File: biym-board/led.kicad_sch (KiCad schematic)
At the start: 3 parts, among them J3 HEADER_01X04_JST_ZH_SMD_VERTI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

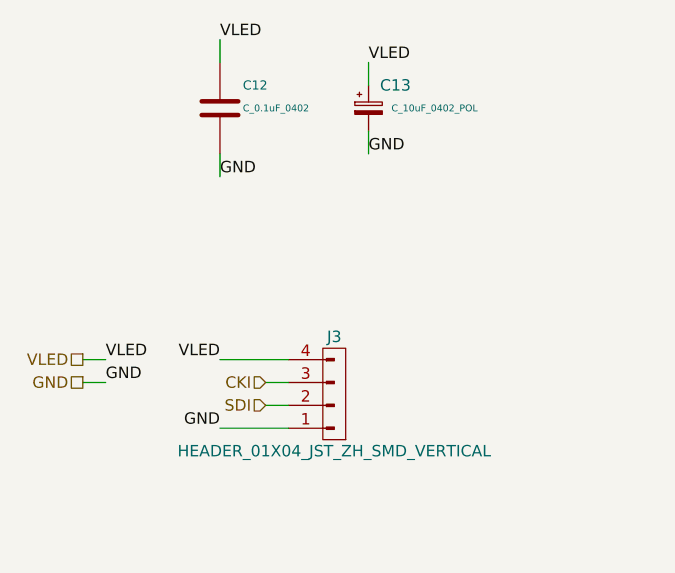
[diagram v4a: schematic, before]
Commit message: Add boost for both led and servo
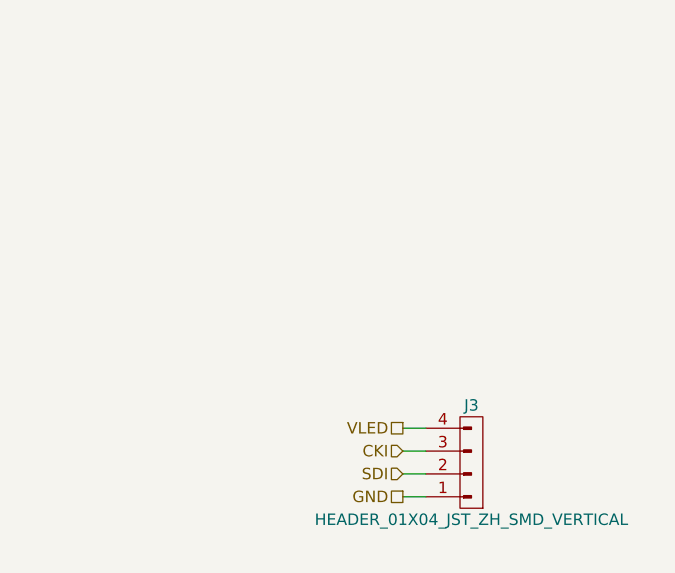
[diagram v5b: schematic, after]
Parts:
- removed C12: C_0.1uF_0402, Janelia:SM0402, symbol Janelia:C_0.1uF_0402
- removed C13: C_10uF_0402_POL, Janelia:SM0402_POL, symbol Janelia:C_10uF_0402_POL
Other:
- moved on the sheet: J3
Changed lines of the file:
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@@
     (company "Peter Polidoro")
   )
-  (wire (pts (xy 119.38 63.5) (xy 119.38 66.04))
+  (wire (pts (xy 139.7 96.52) (xy 142.24 96.52))
     (stroke (width 0) (type default) (color 0 0 0 0))
   )
-  (wire (pts (xy 135.89 60.96) (xy 135.89 63.5))
+  (wire (pts (xy 139.7 93.98) (xy 142.24 93.98))
     (stroke (width 0) (type default) (color 0 0 0 0))
   )
-  (wire (pts (xy 124.46 88.9) (xy 127 88.9))
+  (wire (pts (xy 139.7 99.06) (xy 142.24 99.06))
     (stroke (width 0) (type default) (color 0 0 0 0))
   )
-  (wire (pts (xy 135.89 53.34) (xy 135.89 55.88))
+  (wire (pts (xy 139.7 101.6) (xy 142.24 101.6))
     (stroke (width 0) (type default) (color 0 0 0 0))
   )
-  (wire (pts (xy 104.14 88.9) (xy 106.68 88.9))
-    (stroke (width 0) (type default) (color 0 0 0 0))
-  )
-  (wire (pts (xy 104.14 86.36) (xy 106.68 86.36))
-    (stroke (width 0) (type default) (color 0 0 0 0))
-  )
-  (wire (pts (xy 124.46 91.44) (xy 127 91.44))
-    (stroke (width 0) (type default) (color 0 0 0 0))
-  )
-  (wire (pts (xy 119.38 50.8) (xy 119.38 53.34))
-    (stroke (width 0) (type default) (color 0 0 0 0))
-  )
-  (wire (pts (xy 119.38 86.36) (xy 127 86.36))
-    (stroke (width 0) (type default) (color 0 0 0 0))
-  )
-  (wire (pts (xy 119.38 93.98) (xy 127 93.98))
-    (stroke (width 0) (type default) (color 0 0 0 0))
-  )
-  (label "VLED" (at 135.89 53.34 0)
-    (effects (font (size 1.27 1.27)) (justify left bottom))
-  )
-  (label "VLED" (at 119.38 86.36 180)
-    (effects (font (size 1.27 1.27)) (justify right bottom))
-  )
-  (label "GND" (at 119.38 93.98 180)
-    (effects (font (size 1.27 1.27)) (justify right bottom))
-  )
-  (label "GND" (at 135.89 63.5 0)
-    (effects (font (size 1.27 1.27)) (justify left bottom))
-  )
-  (label "VLED" (at 106.68 86.36 0)
-    (effects (font (size 1.27 1.27)) (justify left bottom))
-  )
-  (label "VLED" (at 119.38 50.8 0)
-    (effects (font (size 1.27 1.27)) (justify left bottom))
-  )
-  (label "GND" (at 119.38 66.04 0)
-    (effects (font (size 1.27 1.27)) (justify left bottom))
-  )
-  (label "GND" (at 106.68 88.9 0)
-    (effects (font (size 1.27 1.27)) (justify left bottom))
-  )
-  (hierarchical_label "VLED" (shape passive) (at 104.14 86.36 180)
+  (hierarchical_label "VLED" (shape passive) (at 139.7 93.98 180)
     (effects (font (size 1.27 1.27)) (justify right))
   )
-  (hierarchical_label "SDI" (shape input) (at 124.46 91.44 180)
+  (hierarchical_label "SDI" (shape input) (at 139.7 99.06 180)
     (effects (font (size 1.27 1.27)) (justify right))
   )
-  (hierarchical_label "GND" (shape passive) (at 104.14 88.9 180)
+  (hierarchical_label "GND" (shape passive) (at 139.7 101.6 180)
     (effects (font (size 1.27 1.27)) (justify right))
   )
-  (hierarchical_label "CKI" (shape input) (at 124.46 88.9 180)
+  (hierarchical_label "CKI" (shape input) (at 139.7 96.52 180)
     (effects (font (size 1.27 1.27)) (justify right))
   )
-  (symbol (lib_id "Janelia:HEADER_01X04_JST_ZH_SMD_VERTICAL") (at 132.08 90.17 180) (unit 1)
+  (symbol (lib_id "Janelia:HEADER_01X04_JST_ZH_SMD_VERTICAL") (at 147.32 97.79 180) (unit 1)
     (in_bom yes) (on_board yes)
-    (property "Reference" "J3" (id 0) (at 132.08 83.82 0))
-    (property "Value" "HEADER_01X04_JST_ZH_SMD_VERTICAL" (id 1) (at 132.08 96.52 0))
-    (property "Footprint" "Janelia:JST_ZH_B4B_ZR_SM4_TF_1x04-1MP_P1.50mm_Vertical" (id 2) (at 132.08 102.87 0)
+    (property "Reference" "J3" (id 0) (at 147.32 91.44 0))
+    (property "Value" "HEADER_01X04_JST_ZH_SMD_VERTICAL" (id 1) (at 147.32 104.14 0))
+    (property "Footprint" "Janelia:JST_ZH_B4B_ZR_SM4_TF_1x04-1MP_P1.50mm_Vertical" (id 2) (at 147.32 110.49 0)
       (effects (font (size 1.27 1.27)) hide)
     )
-    (property "Datasheet" "" (id 3) (at 132.08 91.44 0)
+    (property "Datasheet" "" (id 3) (at 147.32 99.06 0)
       (effects (font (size 1.27 1.27)) hide)
     )
-    (property "Description" "CONN HEADER SMD 4POS 1.5MM" (id 4) (at 132.08 100.33 0)
+    (property "Description" "CONN HEADER SMD 4POS 1.5MM" (id 4) (at 147.32 107.95 0)
       (effects (font (size 1.27 1.27)) hide)
     )
-    (property "Manufacturer" "JST Sales America Inc." (id 5) (at 132.08 107.95 0)
+    (property "Manufacturer" "JST Sales America Inc." (id 5) (at 147.32 115.57 0)
       (effects (font (size 1.27 1.27)) hide)
     )
-    (property "Manufacturer Part Number" "B4B-ZR-SM4-TF(LF)(SN)" (id 6) (at 132.08 105.41 0)
+    (property "Manufacturer Part Number" "B4B-ZR-SM4-TF(LF)(SN)" (id 6) (at 147.32 113.03 0)
       (effects (font (size 1.27 1.27)) hide)
     )
-    (property "Vendor" "Digi-Key" (id 7) (at 132.08 110.49 0)
+    (property "Vendor" "Digi-Key" (id 7) (at 147.32 118.11 0)
       (effects (font (size 1.27 1.27)) hide)
     )
-    (property "Vendor Part Number" "455-1683-1-ND" (id 8) (at 132.08 113.03 0)
+    (property "Vendor Part Number" "455-1683-1-ND" (id 8) (at 147.32 120.65 0)
       (effects (font (size 1.27 1.27)) hide)
     )
@@
     (pin "4")
   )
-  (symbol (lib_id "Janelia:C_0.1uF_0402") (at 119.38 58.42 0) (unit 1)
-    (in_bom yes) (on_board yes)
-    (property "Reference" "C12" (id 0) (at 121.92 55.88 0)
-      (effects (font (size 1.016 1.016)) (justify left))
-    )
-    (property "Value" "C_0.1uF_0402" (id 1) (at 121.92 58.42 0)
-      (effects (font (size 0.762 0.762)) (justify left))
-    )
-    (property "Footprint" "Janelia:SM0402" (id 2) (at 120.3452 62.23 0)
-      (effects (font (size 0.762 0.762)) hide)
-    )
-    (property "Datasheet" "" (id 3) (at 119.38 58.42 0)
-      (effects (font (size 1.524 1.524)) hide)
-    )
-    (property "Vendor" "Digi-Key" (id 4) (at 121.92 53.34 0)
-      (effects (font (size 1.524 1.524)) hide)
-    )
-    (property "Vendor Part Number" "311-1375-1-ND" (id 5) (at 124.46 50.8 0)
-      (effects (font (size 1.524 1.524)) hide)
-    )
-    (property "Description" "CAP CER 0.1UF 25V Y5V" (id 6) (at 127 48.26 0)
-      (effects (font (size 1.524 1.524)) hide)
-    )
-    (property "Package" "0402" (id 7) (at 119.38 58.42 0)
-      (effects (font (size 1.27 1.27)) hide)
-    )
-    (property "Manufacturer" "Yageo" (id 8) (at 119.38 58.42 0)
-      (effects (font (size 1.27 1.27)) hide)
-    )
-    (property "Manufacturer Part Number" "CC0402ZRY5V8BB104" (id 9) (at 119.38 58.42 0)
-      (effects (font (size 1.27 1.27)) hide)
-    )
-    (pin "1")
-    (pin "2")
-  )
-  (symbol (lib_id "Janelia:C_10uF_0402_POL") (at 135.89 58.42 0) (unit 1)
-    (in_bom yes) (on_board yes)
-    (property "Reference" "C13" (id 0) (at 137.16 55.88 0)
-      (effects (font (size 1.27 1.27)) (justify left))
-    )
-    (property "Value" "C_10uF_0402_POL" (id 1) (at 138.43 58.42 0)
-      (effects (font (size 0.762 0.762)) (justify left))
-    )
-    (property "Footprint" "Janelia:SM0402_POL" (id 2) (at 133.604 59.182 0)
-      (effects (font (size 1.524 1.524)) hide)
-    )
-    (property "Datasheet" "" (id 3) (at 136.144 56.642 0)
-      (effects (font (size 1.524 1.524)) hide)
-    )
-    (property "Vendor" "Digi-Key" (id 4) (at 138.684 54.102 0)
-      (effects (font (size 1.524 1.524)) hide)
-    )
-    (property "Vendor Part Number" "478-5343-1-ND" (id 5) (at 141.224 51.562 0)
-      (effects (font (size 1.524 1.524)) hide)
-    )
-    (property "Description" "CAP TANT 10UF 20% 6.3V" (id 6) (at 143.764 49.022 0)
-      (effects (font (size 1.524 1.524)) hide)
-    )
-    (property "Manufacturer" "AVX Corporation" (id 7) (at 135.89 58.42 0)
-      (effects (font (size 1.27 1.27)) hide)
-    )
-    (property "Manufacturer Part Number" "TLCK106M006QTA" (id 8) (at 135.89 58.42 0)
-      (effects (font (size 1.27 1.27)) hide)
-    )
-    (property "Package" "0402" (id 9) (at 135.89 58.42 0)
-      (effects (font (size 1.27 1.27)) hide)
-    )
-    (pin "1")
-    (pin "2")
-  )
 )
